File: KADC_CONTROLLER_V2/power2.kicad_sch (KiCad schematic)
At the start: 49 parts, among them J1 1766343, U14 OKX-T/5-D12N-C, U16 OKX-T/5-D12N-C, U17 AD5274BCPZ-100-RL7, U5 OKX-T/5-D12N-C

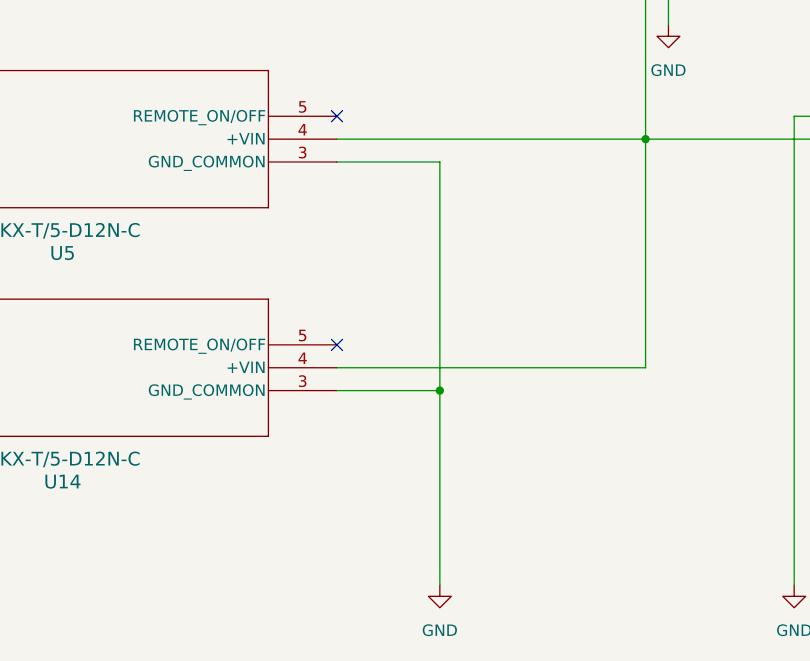
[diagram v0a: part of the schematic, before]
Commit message: Updates SD card on KADC
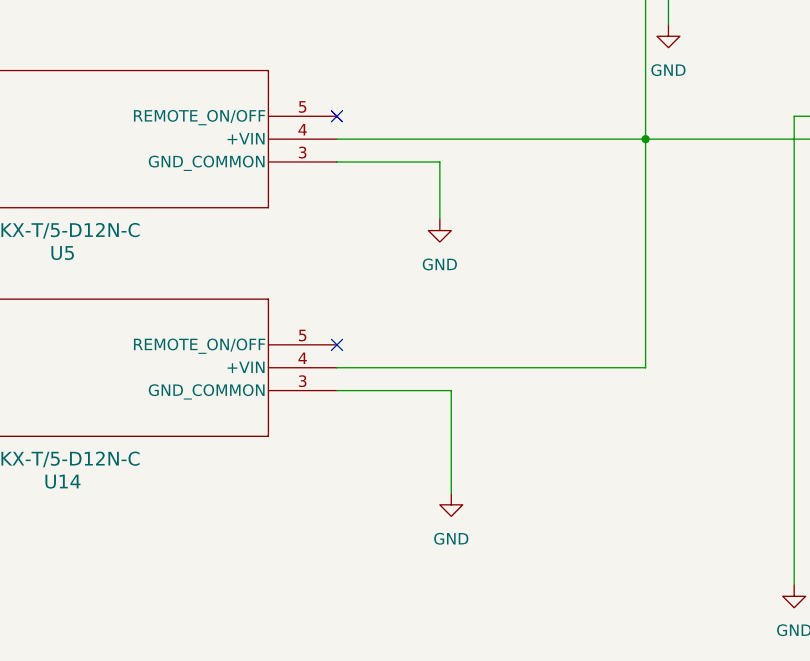
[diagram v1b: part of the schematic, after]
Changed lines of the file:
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@@
 	)
 	(junction
-		(at 120.65 236.22)
-		(diameter 0)
-		(color 0 0 0 0)
-	)
-	(junction
 		(at 121.92 66.04)
 		(diameter 0)
@@
 	(wire
 		(pts
+			(xy 121.92 236.22) (xy 121.92 247.65)
+		)
+		(stroke
+			(width 0)
+			(type default)
+		)
+	)
+	(wire
+		(pts
 			(xy 345.44 220.98) (xy 351.79 220.98)
 		)
@@
 	(wire
 		(pts
-			(xy 387.35 88.9) (xy 393.7 88.9)
+			(xy 120.65 210.82) (xy 120.65 217.17)
 		)
 		(stroke
@@
 	(wire
 		(pts
-			(xy 120.65 210.82) (xy 120.65 236.22)
+			(xy 387.35 88.9) (xy 393.7 88.9)
 		)
 		(stroke
@@
 	(wire
 		(pts
-			(xy 121.92 66.04) (xy 121.92 74.93)
+			(xy 109.22 236.22) (xy 121.92 236.22)
 		)
 		(stroke
@@
 	(wire
 		(pts
-			(xy 34.29 147.32) (xy 38.1 147.32)
+			(xy 121.92 66.04) (xy 121.92 74.93)
 		)
 		(stroke
@@
 	(wire
 		(pts
-			(xy 121.92 88.9) (xy 130.81 88.9)
+			(xy 34.29 147.32) (xy 38.1 147.32)
 		)
 		(stroke
@@
 	(wire
 		(pts
-			(xy 109.22 236.22) (xy 120.65 236.22)
+			(xy 121.92 88.9) (xy 130.81 88.9)
 		)
 		(stroke
@@
 	(wire
 		(pts
-			(xy 120.65 236.22) (xy 120.65 257.81)
-		)
-		(stroke
-			(width 0)
-			(type default)
-		)
-	)
-	(wire
-		(pts
 			(xy 72.39 147.32) (xy 72.39 151.13)
 		)
@@
 	(symbol
 		(lib_id "power:GND")
-		(at 120.65 257.81 0)
+		(at 120.65 217.17 0)
 		(unit 1)
 		(body_style 1)
@@
 		(fields_autoplaced yes)
 		(property "Reference" "#PWR021"
-			(at 120.65 264.16 0)
+			(at 120.65 223.52 0)
 			(hide yes)
 			(show_name no)
@@
 		)
 		(property "Value" "GND"
-			(at 120.65 262.89 0)
+			(at 120.65 222.25 0)
 			(show_name no)
 			(do_not_autoplace no)
@@
 		)
 		(property "Footprint" ""
-			(at 120.65 257.81 0)
+			(at 120.65 217.17 0)
 			(hide yes)
 			(show_name no)
@@
 		)
 		(property "Datasheet" ""
-			(at 120.65 257.81 0)
+			(at 120.65 217.17 0)
 			(hide yes)
 			(show_name no)
@@
 		)
 		(property "Description" "Power symbol creates a global label with name \"GND\" , ground"
-			(at 120.65 257.81 0)
+			(at 120.65 217.17 0)
 			(hide yes)
 			(show_name no)
@@
 					(unit 1)
 				)
+			)
+		)
+	)
+	(symbol
+		(lib_id "power:GND")
+		(at 121.92 247.65 0)
+		(unit 1)
+		(body_style 1)
+		(exclude_from_sim no)
+		(in_bom yes)
+		(on_board yes)
+		(in_pos_files yes)
+		(dnp no)
+		(fields_autoplaced yes)
+		(property "Reference" "#PWR0122"
+			(at 121.92 254 0)
+			(hide yes)
+			(show_name no)
+			(do_not_autoplace no)
+			(effects
+				(font
+					(size 1.27 1.27)
+				)
+			)
+		)
+		(property "Value" "GND"
+			(at 121.92 252.73 0)
+			(show_name no)
+			(do_not_autoplace no)
+			(effects
+				(font
+					(size 1.27 1.27)
+				)
+			)
+		)
+		(property "Footprint" ""
+			(at 121.92 247.65 0)
+			(hide yes)
+			(show_name no)
+			(do_not_autoplace no)
+			(effects
+				(font
+					(size 1.27 1.27)
+				)
+			)
+		)
+		(property "Datasheet" ""
+			(at 121.92 247.65 0)
+			(hide yes)
+			(show_name no)
+			(do_not_autoplace no)
+			(effects
+				(font
+					(size 1.27 1.27)
+				)
+			)
+		)
+		(property "Description" "Power symbol creates a global label with name \"GND\" , ground"
+			(at 121.92 247.65 0)
+			(hide yes)
+			(show_name no)
+			(do_not_autoplace no)
+			(effects
+				(font
+					(size 1.27 1.27)
+				)
+			)
+		)
+		(pin "1"
+		)
+		(instances
+			(project "PSEC5_Ctrl_Board"
+				(path "/165f2ae6-d522-4adf-a6c4-bb137b209d33/ba7b9281-d70b-432c-9c7d-bfda745e0250"
+					(reference "#PWR0122")
+					(unit 1)
+				)
